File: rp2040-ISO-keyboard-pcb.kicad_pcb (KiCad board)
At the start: 2 copper layers, 347.7 x 125.4 mm, 350 parts, among them J1 USB_C_Receptacle_USB2.0, J2 Conn_01x04, SW1 SW_HS, SW10 SW_HS, SW11 SW_HS, SW12 SW_HS, SW13 SW_HS, SW14 SW_HS, SW15 SW_HS, SW16 SW_HS, SW17 SW_HS, SW18 SW_HS, SW19 SW_HS, SW2 SW_HS, SW20 SW_HS, SW21 SW_HS, SW22 SW_HS, SW23 SW_HS, SW24 SW_HS, SW25 SW_HS, SW26 SW_HS, SW27 SW_HS, SW28 SW_HS, SW29 SW_HS, SW3 SW_HS, SW30 SW_HS, SW31 SW_HS, SW32 SW_HS, SW33 SW_HS, SW34 SW_HS, SW35 SW_HS, SW36 SW_HS, SW37 SW_HS, SW38 SW_HS, SW39 SW_HS, SW4 SW_HS, SW40 SW_HS, SW41 SW_HS, SW42 SW_HS, SW43 SW_HS, SW44 SW_HS, SW45 SW_HS, SW46 SW_HS, SW47 SW_HS, SW48 SW_HS, SW49 SW_HS, SW5 SW_HS, SW50 SW_HS, SW51 SW_HS, SW52 SW_HS, SW53 SW_HS, SW54 SW_HS, SW55 SW_HS, SW56 SW_HS, SW57 SW_HS, SW58 SW_HS, SW59 SW_HS, SW6 SW_HS, SW60 SW_HS, SW61 SW_HS, SW62 SW_HS, SW63 SW_HS, SW64 SW_HS, SW65 SW_HS, SW66 SW_HS, SW67 SW_HS, SW68 SW_HS, SW69 SW_HS, SW7 SW_HS, SW70 SW_HS, SW71 SW_HS, SW72 SW_HS, SW73 SW_HS, SW74 SW_HS, SW75 SW_HS, SW76 SW_HS, SW77 SW_HS, SW78 SW_HS, SW79 SW_HS, SW8 SW_HS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

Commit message: *now finished routing (zones left)
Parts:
- moved C10 0.90 mm to (-122.3, -239.2)
- moved C4 0.90 mm to (-122.3, -240.3)
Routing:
- net Net-(R1-Pad2): track 2.55 -> 37.1 mm, vias 0 -> 2
- net +1V1: track 8.39 -> 9.05 mm

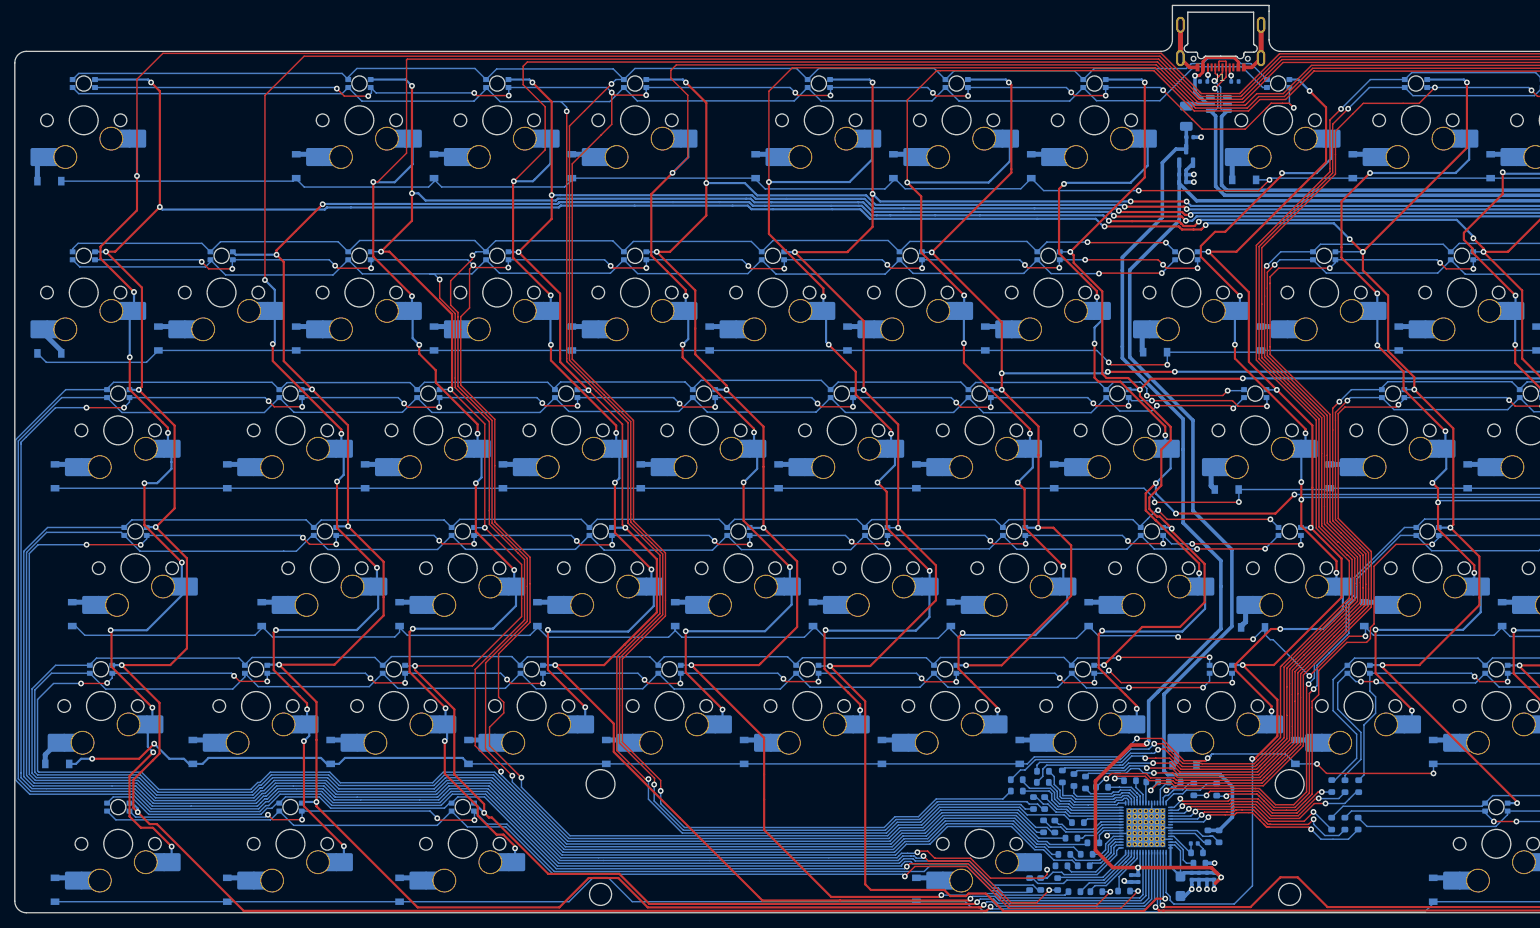
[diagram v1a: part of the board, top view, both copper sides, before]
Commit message: cleaned up some routing and used smaller resistors (0402 instead of 0603)
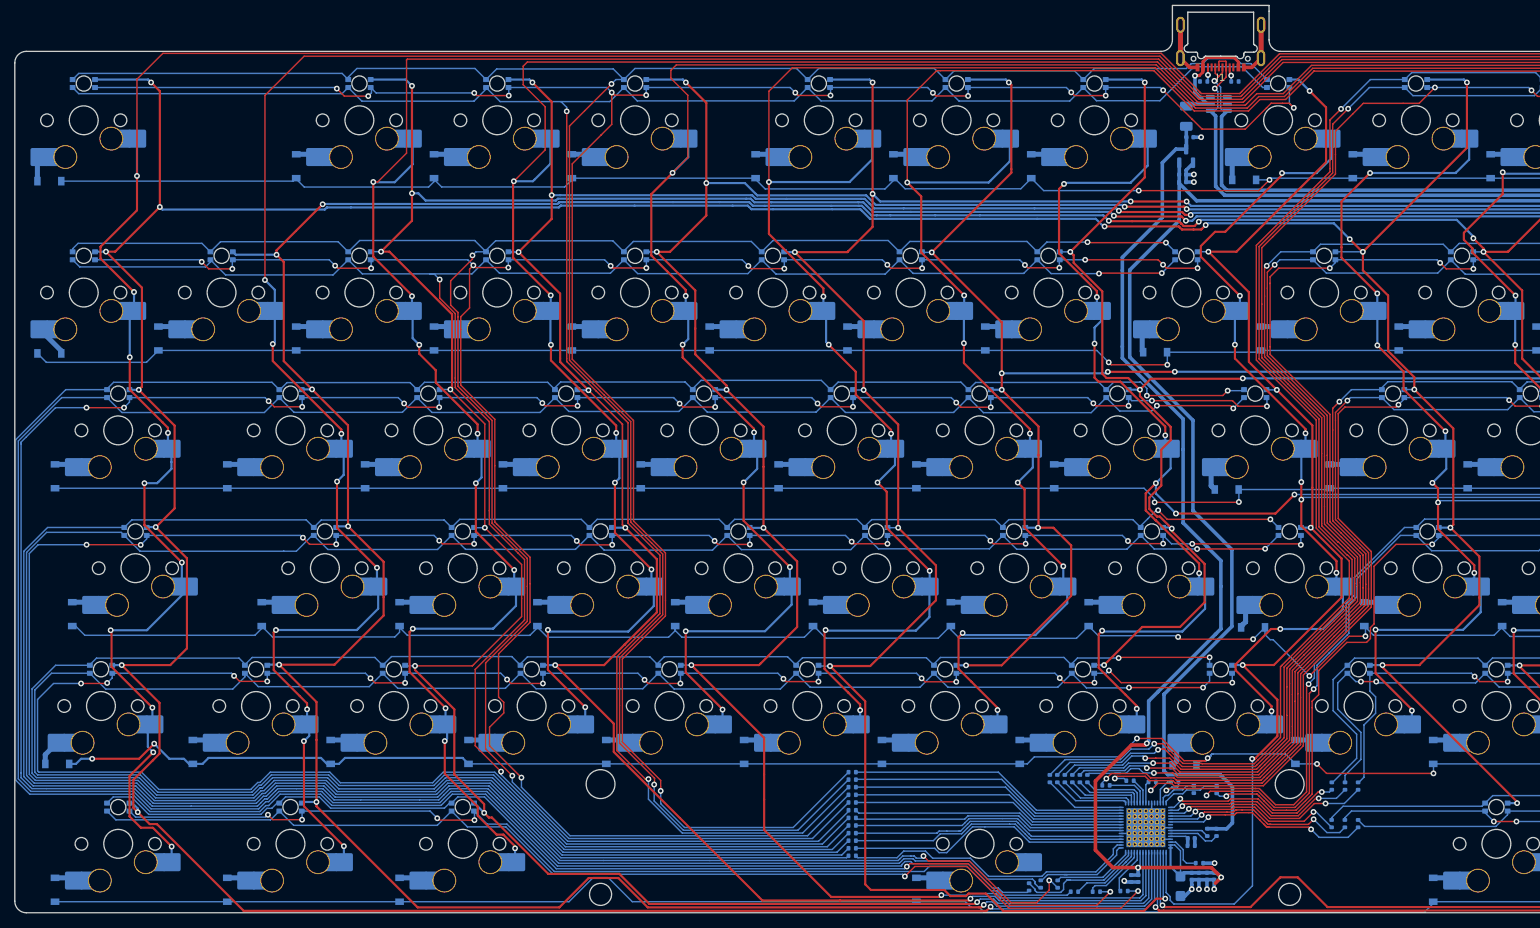
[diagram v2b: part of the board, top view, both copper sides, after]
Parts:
- R10, R11, R13, R14, R16, R17, R18, R19, R2, R20, R21, R22, R23, R24, R25, R26, R27, R28, R29, R3, R30, R31, R32, R33, R34, R35, R36, R37, R38, R39, R40, R41, R42, R43, R44, R45, R6, R7, R8, R9: footprint Resistor_SMD:R_0603_1608Metric -> Resistor_SMD:R_0402_1005Metric
- moved R35 33.4 mm to (-300.2, -215.3)
- moved R34 32.5 mm to (-300.2, -214.2)
- moved R29 32.1 mm to (-300.2, -212.1)
- moved R18 31.4 mm to (-300.2, -219.5)
- moved R36 30.4 mm to (-300.2, -216.3)
- moved R30 29.4 mm to (-300.2, -213.2)
- moved R28 29.0 mm to (-300.2, -211.1)
- moved R16 28.2 mm to (-300.2, -218.4), turned to 180 degrees
- moved R6 26.8 mm to (-300.2, -221.6), turned to 180 degrees
- moved R17 26.5 mm to (-300.2, -217.4), turned to 180 degrees
- moved R7 25.2 mm to (-300.2, -220.6), turned to 180 degrees
- moved R8 22.9 mm to (-300.2, -222.6)
- moved R9 4.57 mm to (-272.9, -221.7), turned to 90 degrees
- moved R14 3.08 mm to (-270.8, -221.7), turned to 90 degrees
- moved R11 2.22 mm to (-271.8, -221.7), turned to 90 degrees
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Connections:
- R11 pad 1: Net-(R11-Pad1) -> Net-(U3-Pad46)
- R14 pad 1: Net-(R14-Pad1) -> Net-(U3-Pad47)
- U3 pad 46: Net-(R14-Pad1) -> Net-(U3-Pad46)
- U3 pad 47: Net-(R11-Pad1) -> Net-(U3-Pad47)
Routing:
- net CS20: track 375.2 -> 340.0 mm
- net CS26: track 345.3 -> 310.3 mm
- net CS25: track 340.7 -> 306.0 mm
- net Net-(R35-Pad1): track 4.35 -> 37.8 mm
- net Net-(R29-Pad1): track 6.24 -> 39.3 mm
- net Net-(R34-Pad1): track 5.44 -> 38.2 mm
- net Net-(R18-Pad1): track 5.37 -> 38.1 mm
- net CS21: track 374.9 -> 343.1 mm
- net CS27: track 344.1 -> 312.7 mm
- net Net-(R28-Pad1): track 9.63 -> 40.9 mm
- net CS9: track 328.6 -> 297.6 mm
- net Net-(R36-Pad1): track 6.66 -> 37.6 mm
- net CS19: track 367.0 -> 336.8 mm, vias 4 -> 2
- net Net-(R30-Pad1): track 9.11 -> 38.5 mm
- net CS7: track 328.0 -> 298.6 mm
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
